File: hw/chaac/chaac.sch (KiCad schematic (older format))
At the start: 70 parts, among them J1 Solar, J2 Battery, J3 TC2030-CTX, J5 windrain, Q1 Q_PMOS_GSD, U1 TPS7A0530PDBVT, U2 MCP73871, U3 STM32L412K, U4 DPS368, U5 SHT3x-DIS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

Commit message: Update part numbers?
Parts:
- AE1: DKPN (none) -> 343-ANT-916-HESM-ND; MPN (none) -> ANT-916-HESM
- C1, C2: DKPN (none) -> 1276-3063-1-ND; MPN (none) -> CL31A476MPHNNNE
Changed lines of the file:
@@
 F 2 "alvarop:ANT-916-HESM" H 12700 8800 50  0001 C CNN
 F 3 "~" H 12700 8800 50  0001 C CNN
+F 4 "343-ANT-916-HESM-ND" H 12700 8800 50  0001 C CNN "DKPN"
+F 5 "ANT-916-HESM" H 12700 8800 50  0001 C CNN "MPN"
 	1    12700 8800
 	1    0    0    -1
@@
 F 2 "Capacitor_SMD:C_1206_3216Metric" H 2400 1500 50  0001 C CNN
 F 3 "~" H 2400 1500 50  0001 C CNN
+F 4 "1276-3063-1-ND" H 2400 1500 50  0001 C CNN "DKPN"
+F 5 "CL31A476MPHNNNE" H 2400 1500 50  0001 C CNN "MPN"
 	1    2400 1500
 	1    0    0    -1
@@
 F 2 "Capacitor_SMD:C_1206_3216Metric" H 2800 1500 50  0001 C CNN
 F 3 "~" H 2800 1500 50  0001 C CNN
+F 4 "1276-3063-1-ND" H 2800 1500 50  0001 C CNN "DKPN"
+F 5 "CL31A476MPHNNNE" H 2800 1500 50  0001 C CNN "MPN"
 	1    2800 1500
 	1    0    0    -1

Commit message: Committing chaac v6.1 files I forgot to :(
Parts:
- removed AE1: Antenna, alvarop:ANT-916-HESM, symbol Device:Antenna
- added AE1: Antenna_Chip, alvarop:W3211, symbol Device:Antenna_Chip
- U3: footprint alvarop:UFQFPN32_ALT -> alvarop:UFQFPN32-ALT; DKPN (none) -> 497-18230-ND; MPN (none) -> STM32L412KBU6
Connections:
- net GND: now also AE1.2 (PCB_Trace)
- net at C16.1, L1.2: now also AE1.1 (FEED)
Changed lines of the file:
@@
 Sheet 1 1
 Title "Chaac"
-Date "2020-12-06"
-Rev "6.0"
+Date "2021-02-22"
+Rev "6.1"
 Comp "@alvaroprieto"
 Comment1 ""
@@
 F 0 "U3" H 6900 7300 50  0000 C CNN
 F 1 "STM32L412K" H 7000 5300 50  0000 C CNN
-F 2 "alvarop:UFQFPN32_ALT" V 6800 6100 50  0001 C CNN
+F 2 "alvarop:UFQFPN32-ALT" V 6800 6100 50  0001 C CNN
 F 3 "" V 6800 6100 50  0001 C CNN
+F 4 "497-18230-ND" H 7300 6100 50  0001 C CNN "DKPN"
+F 5 "STM32L412KBU6" H 7300 6100 50  0001 C CNN "MPN"
 	1    7300 6100
 	1    0    0    -1
@@
 	7600 2500 8000 2500
 $Comp
-L Device:Antenna AE1
-U 1 1 6109FCC0
-P 12700 8800
-F 0 "AE1" H 12780 8789 50  0000 L CNN
-F 1 "Antenna" H 12780 8698 50  0000 L CNN
-F 2 "alvarop:ANT-916-HESM" H 12700 8800 50  0001 C CNN
-F 3 "~" H 12700 8800 50  0001 C CNN
-F 4 "343-ANT-916-HESM-ND" H 12700 8800 50  0001 C CNN "DKPN"
-F 5 "ANT-916-HESM" H 12700 8800 50  0001 C CNN "MPN"
-	1    12700 8800
-	1    0    0    -1
-$EndComp
-$Comp
 L Device:C_Small C14
 U 1 1 610BC956
@@
 Wire Wire Line
 	7600 9500 8000 9500
+$Comp
+L Device:Antenna_Chip AE1
+U 1 1 6024F558
+P 12800 8800
+F 0 "AE1" H 12980 8927 50  0000 L CNN
+F 1 "Antenna_Chip" H 12980 8836 50  0000 L CNN
+F 2 "alvarop:W3211" H 12700 8975 50  0001 C CNN
+F 3 "~" H 12700 8975 50  0001 C CNN
+	1    12800 8800
+	1    0    0    -1
+$EndComp
+Wire Wire Line
+	12700 8900 12700 9000
+$Comp
+L power:GND #PWR07
+U 1 1 6027BDC4
+P 12900 9000
+F 0 "#PWR07" H 12900 8750 50  0001 C CNN
+F 1 "GND" H 12905 8827 50  0000 C CNN
+F 2 "" H 12900 9000 50  0001 C CNN
+F 3 "" H 12900 9000 50  0001 C CNN
+	1    12900 9000
+	1    0    0    -1
+$EndComp
+Wire Wire Line
+	12900 9000 12900 8900
 $EndSCHEMATC

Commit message: Released chaac v6.2 to JLCPCB
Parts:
- removed AE1: Antenna_Chip, alvarop:W3211, symbol Device:Antenna_Chip
- removed C14, C16: DNP, Capacitor_SMD:C_0402_1005Metric, symbol Device:C_Small
- removed L1: 0, Inductor_SMD:L_0402_1005Metric, symbol Device:L_Small
- added R26: 10k, Resistor_SMD:R_0402_1005Metric, symbol Device:R_Small
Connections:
- net GND: now also R26.2
- net LED1: now also R26.1
- no-connect marks 11 -> 12
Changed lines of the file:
@@
 Sheet 1 1
 Title "Chaac"
-Date "2021-02-22"
-Rev "6.1"
+Date "2021-06-13"
+Rev "6.2"
 Comp "@alvaroprieto"
 Comment1 ""
@@
 	1    0    0    -1
 $EndComp
-$Comp
-L power:GND #PWR0107
-U 1 1 602C1B09
-P 12100 9300
-F 0 "#PWR0107" H 12100 9050 50  0001 C CNN
-F 1 "GND" H 12105 9127 50  0000 C CNN
-F 2 "" H 12100 9300 50  0001 C CNN
-F 3 "" H 12100 9300 50  0001 C CNN
-	1    12100 9300
-	1    0    0    -1
-$EndComp
 Text Label 8600 5200 2    50   ~ 0
 WDIR
@@
 WSPEED
 Wire Wire Line
-	6000 6600 6700 6600
+	6000 6600 6300 6600
 Wire Wire Line
 	6700 5700 6400 5700
@@
 	7600 2500 8000 2500
 $Comp
-L Device:C_Small C14
-U 1 1 610BC956
-P 12100 9100
-F 0 "C14" H 11900 9100 50  0000 L CNN
-F 1 "DNP" H 11800 9000 50  0000 L CNN
-F 2 "Capacitor_SMD:C_0402_1005Metric" H 12100 9100 50  0001 C CNN
-F 3 "~" H 12100 9100 50  0001 C CNN
-	1    12100 9100
-	1    0    0    -1
-$EndComp
-$Comp
-L Device:C_Small C16
-U 1 1 610BCF40
-P 12500 9100
-F 0 "C16" H 12592 9146 50  0000 L CNN
-F 1 "DNP" H 12592 9055 50  0000 L CNN
-F 2 "Capacitor_SMD:C_0402_1005Metric" H 12500 9100 50  0001 C CNN
-F 3 "~" H 12500 9100 50  0001 C CNN
-	1    12500 9100
-	1    0    0    -1
-$EndComp
-$Comp
-L Device:L_Small L1
-U 1 1 610BE712
-P 12300 9000
-F 0 "L1" V 12485 9000 50  0000 C CNN
-F 1 "0" V 12394 9000 50  0000 C CNN
-F 2 "Inductor_SMD:L_0402_1005Metric" H 12300 9000 50  0001 C CNN
-F 3 "~" H 12300 9000 50  0001 C CNN
-	1    12300 9000
-	0    -1   -1   0
-$EndComp
-Wire Wire Line
-	12200 9000 12100 9000
-Connection ~ 12100 9000
-Wire Wire Line
-	12400 9000 12500 9000
-$Comp
-L power:GND #PWR0115
-U 1 1 6110C8BA
-P 12500 9300
-F 0 "#PWR0115" H 12500 9050 50  0001 C CNN
-F 1 "GND" H 12505 9127 50  0000 C CNN
-F 2 "" H 12500 9300 50  0001 C CNN
-F 3 "" H 12500 9300 50  0001 C CNN
-	1    12500 9300
-	1    0    0    -1
-$EndComp
-Wire Wire Line
-	12500 9000 12700 9000
-Connection ~ 12500 9000
-Wire Wire Line
-	12100 9300 12100 9200
-Wire Wire Line
-	12500 9300 12500 9200
-$Comp
 L Device:C_Small C1
 U 1 1 6129CD31
@@
 $EndComp
 Wire Wire Line
-	10800 9000 12100 9000
-Wire Wire Line
 	6700 6100 6000 6100
 Wire Wire Line
@@
 	7600 9500 8000 9500
 $Comp
-L Device:Antenna_Chip AE1
-U 1 1 6024F558
-P 12800 8800
-F 0 "AE1" H 12980 8927 50  0000 L CNN
-F 1 "Antenna_Chip" H 12980 8836 50  0000 L CNN
-F 2 "alvarop:W3211" H 12700 8975 50  0001 C CNN
-F 3 "~" H 12700 8975 50  0001 C CNN
-	1    12800 8800
-	1    0    0    -1
-$EndComp
-Wire Wire Line
-	12700 8900 12700 9000
-$Comp
-L power:GND #PWR07
-U 1 1 6027BDC4
-P 12900 9000
-F 0 "#PWR07" H 12900 8750 50  0001 C CNN
-F 1 "GND" H 12905 8827 50  0000 C CNN
-F 2 "" H 12900 9000 50  0001 C CNN
-F 3 "" H 12900 9000 50  0001 C CNN
-	1    12900 9000
-	1    0    0    -1
-$EndComp
-Wire Wire Line
-	12900 9000 12900 8900
+L Device:R_Small R26
+U 1 1 60C86401
+P 6300 6800
+F 0 "R26" V 6400 6850 50  0000 R CNN
+F 1 "10k" V 6200 6850 50  0000 R CNN
+F 2 "Resistor_SMD:R_0402_1005Metric" H 6300 6800 50  0001 C CNN
+F 3 "~" H 6300 6800 50  0001 C CNN
+F 4 "311-10KJRCT-ND" H 4050 -3400 50  0001 C CNN "DKPN"
+F 5 "RC0402JR-0710KL" H 4050 -3400 50  0001 C CNN "MPN"
+	1    6300 6800
+	1    0    0    -1
+$EndComp
+Wire Wire Line
+	6300 6700 6300 6600
+Connection ~ 6300 6600
+Wire Wire Line
+	6300 6600 6700 6600
+$Comp
+L power:GND #PWR0107
+U 1 1 60CA867F
+P 6300 7000
+F 0 "#PWR0107" H 6300 6750 50  0001 C CNN
+F 1 "GND" H 6305 6827 50  0000 C CNN
+F 2 "" H 6300 7000 50  0001 C CNN
+F 3 "" H 6300 7000 50  0001 C CNN
+	1    6300 7000
+	1    0    0    -1
+$EndComp
+Wire Wire Line
+	6300 7000 6300 6900
+NoConn ~ 10800 9000
 $EndSCHEMATC

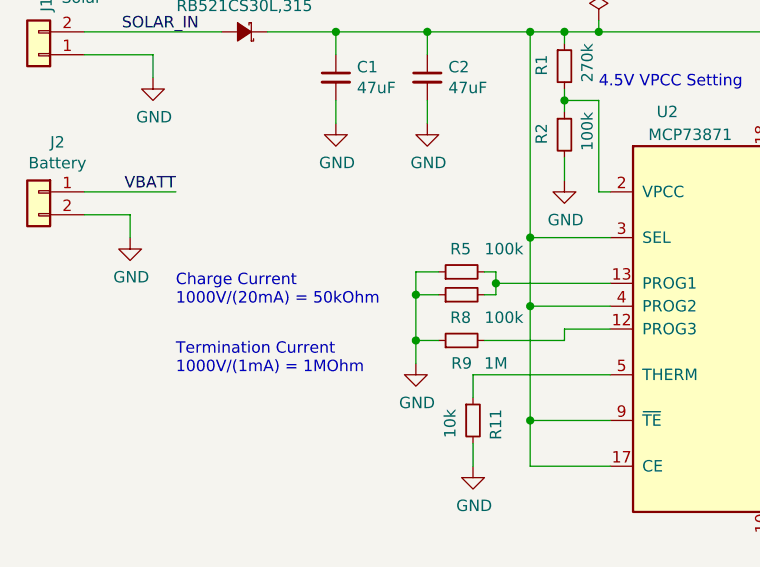
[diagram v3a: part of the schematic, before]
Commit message: Changed resistors for charger to get 200mA charge rate
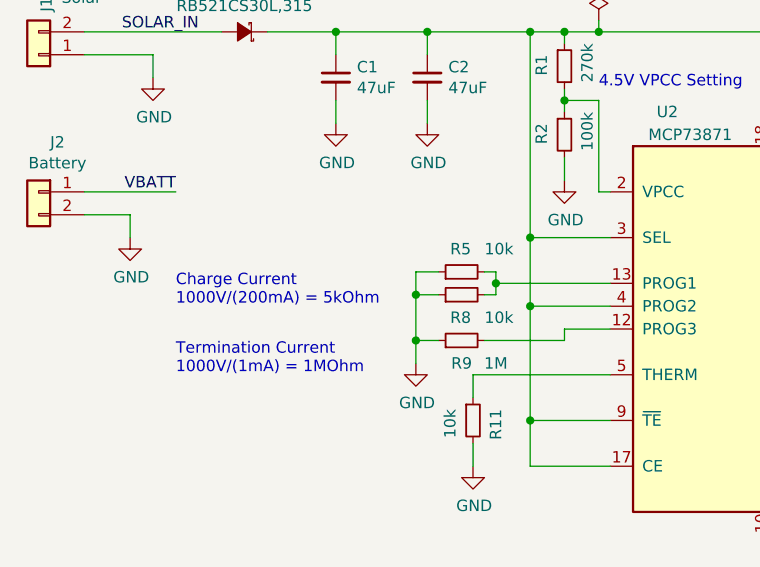
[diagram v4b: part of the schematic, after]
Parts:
- R5, R8: value 100k -> 10k
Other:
- note added: "Charge Current\n1000V/(200mA) = 5kOhm"
- note removed: "Charge Current\n1000V/(20mA) = 50kOhm"
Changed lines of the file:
@@
 Sheet 1 1
 Title "Chaac"
-Date "2021-06-13"
-Rev "6.2"
+Date "2021-07-03"
+Rev "6.3"
 Comp "@alvaroprieto"
 Comment1 ""
@@
 $EndComp
 Text Notes 1700 2500 0    50   ~ 0
-Charge Current\n1000V/(20mA) = 50kOhm
+Charge Current\n1000V/(200mA) = 5kOhm
 $Comp
 L Device:R_Small R5
@@
 P 2950 2350
 F 0 "R5" V 3050 2400 50  0000 R CNN
-F 1 "100k" V 3050 2250 50  0000 R CNN
+F 1 "10k" V 3050 2250 50  0000 R CNN
 F 2 "Resistor_SMD:R_0402_1005Metric" H 2950 2350 50  0001 C CNN
 F 3 "~" H 2950 2350 50  0001 C CNN
@@
 P 2950 2450
 F 0 "R8" V 2850 2500 50  0000 R CNN
-F 1 "100k" V 2850 2350 50  0000 R CNN
+F 1 "10k" V 2850 2350 50  0000 R CNN
 F 2 "Resistor_SMD:R_0402_1005Metric" H 2950 2450 50  0001 C CNN
 F 3 "~" H 2950 2450 50  0001 C CNN
